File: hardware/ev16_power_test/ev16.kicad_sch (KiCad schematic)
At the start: 179 parts, among them CN1 Conn_05x02_Female, CN2 PJ-242, J1 USB_C_Receptacle, J10 Conn_01x03_Pin, J11 Conn_02x05_Counter_Clockwise, J2 Conn_01x02_Socket, J3 AudioJack4, J4 Conn_02x03_Odd_Even, J5 Conn_02x03_Odd_Even, J6 Conn_02x05_Counter_Clockwise, J7 Conn_02x05_Counter_Clockwise, J8 Conn_02x05_Counter_Clockwise, J9 Conn_02x05_Counter_Clockwise, Q1 2N7002, Q2 2N7002, Q3 2N7002, SW1 SW_SPDT, SW2 SW_Push, SW3 SW_Push, SW4 SW_Push, SW5 SW_Push, SW6 SW_Push, SW7 SW_Push, U1 BQ21040DBV, U10 STM32F405RGTx, U2 USBLC6-2P6, U3 STM32F072CBTx, U4 CH340C, U5 TPS63060, U6 WM8960CGEFL/RV, U7 ESP32-S3-WROOM-1, U8 M24C02-RMN6TP, U9 AMS1117-3.3, Y1 Crystal_GND24

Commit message: New linear regulator, ideal diodes, began working on the layout
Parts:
- removed C51, C52: 10u, Capacitor_SMD:C_0402_1005Metric, symbol Device:C
- removed D2, D3: 1N5819WS, Diode_SMD:D_SOD-323, symbol Device:D_Schottky
- removed J10: Conn_01x03_Pin, Connector_PinSocket_2.54mm:PinSocket_1x03_P2.54mm_Vertical_SMD_Pin1Left, symbol Connector:Conn_01x03_Pin
- removed U9: AMS1117-3.3, Package_TO_SOT_SMD:SOT-223-3_TabPin2, symbol Regulator_Linear:AMS1117-3.3
- added R47: 10k, Resistor_SMD:R_0402_1005Metric, symbol Device:R_Small_US
- added R53: 15k, Resistor_SMD:R_0402_1005Metric, symbol Device:R_Small_US
- added TP10, TP7, TP8, TP9: TestPoint, TestPoint:TestPoint_Pad_2.0x2.0mm, symbol Connector:TestPoint
- added U11: ME6211C28M5, Package_TO_SOT_SMD:SOT-23-5, symbol Regulator_Linear:ME6211C28M5
- added U9: TPS2116DRL, Package_TO_SOT_SMD:SOT-583-8, symbol Power_Management:TPS2116DRL
- C18, C7: value 10u -> 1u; JLCPCB Part # C307415 -> C52923
- TP1, TP2, TP3, TP4, TP5, TP6: footprint TestPoint:TestPoint_Pad_4.0x4.0mm -> TestPoint:TestPoint_Pad_2.0x2.0mm
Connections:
- net +3.3V: now also C7.1, U11.1 (V_{IN}), U11.3 (CE)
- net GND: now also R47.1, TP7.1, U11.2 (V_{SS}), U9.1 (GND)
- net GNDA: now also TP10.1
- net HP_L: now also TP8.1
- net MIC_P: now also TP9.1
- net VBUS: now also R53.2, U9.3 (VIN1), U9.5 (MODE)
- net at C12.1, J2.2 (Pin_2), R11.1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: now also U9.6 (VIN2)
- net VSYS: now reaches SW1.2 (B)
- net VSYS: now also R12.2, R14.1, TP3.1
- net at C18.1, L1.1: now also U11.5 (V_{OUT})
- new net: SW1.3 (C), U9.2 (VOUT), U9.7 (VOUT)
- new net: R47.2, R53.1, U9.4 (PR1)
- no-connect marks 57 -> 58
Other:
- note added: "BATTERY"
- moved on the sheet: C10, C11, C12, C14, C15, C16, C19, C20, C22, C24, C27, C29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

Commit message: finished laying out the board with the power changes
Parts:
- removed L1: 120Ω, Inductor_SMD:L_0603_1608Metric, symbol Device:FerriteBead
- added C51, C52: 100n, Capacitor_SMD:C_0402_1005Metric, symbol Device:C_Small
- added J10: Conn_01x03_Pin, Connector_PinHeader_1.00mm:PinHeader_1x03_P1.00mm_Vertical, symbol Connector:Conn_01x03_Socket
- C10: value 1u -> 100n; symbol Device:C -> Device:C_Small; JLCPCB Part # C52923 -> C85866
- C11: value 10n -> 100n; footprint Capacitor_SMD:C_0402_1005Metric -> Capacitor_SMD:C_0402_1005Metri; symbol Device:C -> Device:C_Small; JLCPCB Part # C15195 -> C85866
- C18, C7: symbol Device:C -> Device:C_Small
- C24, C27, C29, C30, C31, C35: value 10u -> 22u; JLCPCB Part # C17024 -> C5674
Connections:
- net +3.3V: now also U10.13 (VDDA), J10.1 (Pin_1); no longer C7.1, U11.1 (V_{IN}), U11.3 (CE)
- net +3.3VA: no longer U10.13 (VDDA)
- net GND: now also C51.2, C52.2; no longer C18.2, U11.2 (V_{SS})
- net GNDA: now also C18.2, U11.2 (V_{SS})
- net VSYS: now also J10.3 (Pin_3)
- net at C10.1, C11.1, R52.1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: now also C18.1, U11.5 (V_{OUT})
- new net: C51.1, C52.1, C7.1, J10.2 (Pin_2), U11.1 (V_{IN}), U11.3 (CE)
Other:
- moved on the sheet: C10, C11, C18, C7, NT1, R52, TP1, TP2, U11

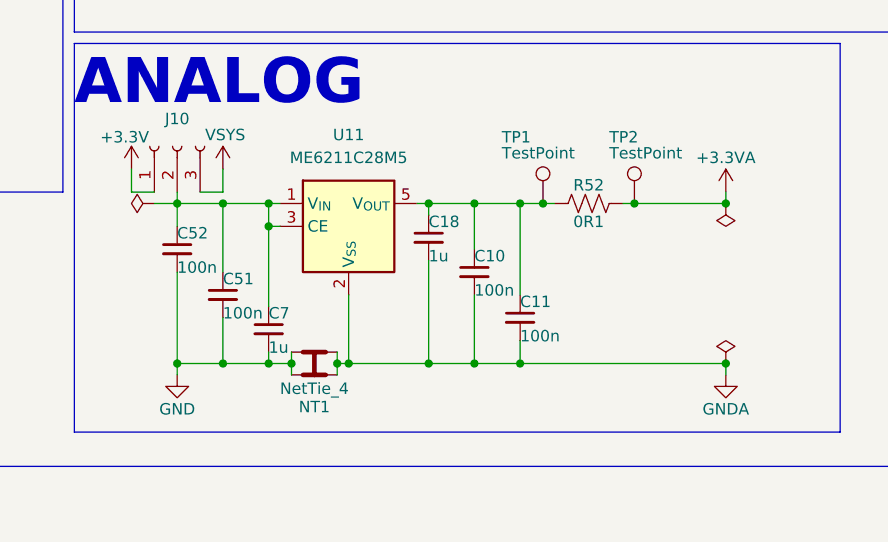
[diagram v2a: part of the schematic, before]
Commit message: Removed extra caps from linear power supply that wasn't needed
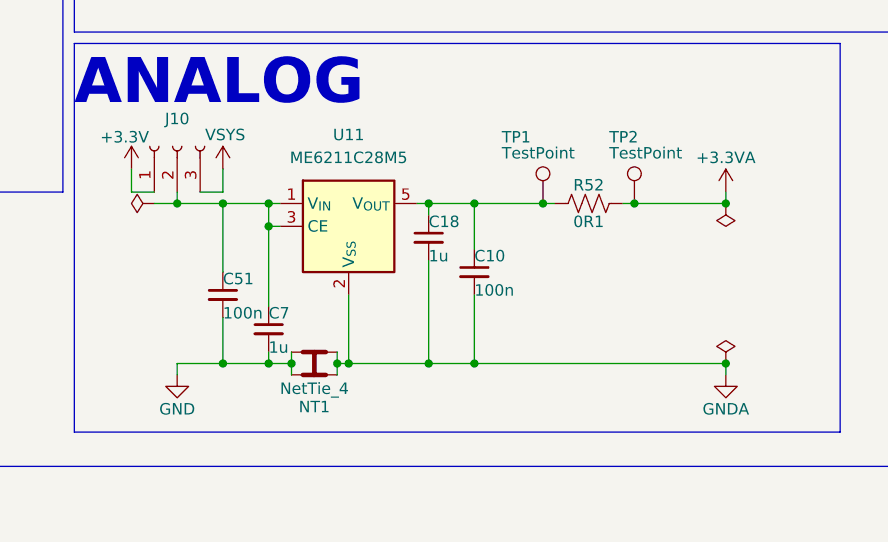
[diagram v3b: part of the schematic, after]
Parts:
- removed C11: 100n, Capacitor_SMD:C_0402_1005Metri, symbol Device:C_Small
- removed C52: 100n, Capacitor_SMD:C_0402_1005Metric, symbol Device:C_Small

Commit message: Changed linear regulator to XC6227C301MR-G and made a symbol for it. Added heat sink areas for the analog regulator
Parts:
- removed TP1, TP10, TP2, TP3, TP4, TP5, TP6, TP7, TP8, TP9: TestPoint, TestPoint:TestPoint_Pad_2.0x2.0mm, symbol Connector:TestPoint
- removed U11: ME6211C28M5, Package_TO_SOT_SMD:SOT-23-5, symbol Regulator_Linear:ME6211C28M5
- added J12, J13, J14, J15, J16, J17, J18, J19, J20, J21: Conn_01x01, Connector_PinHeader_2.54mm:PinHeader_1x01_P2.54mm_Vertical, symbol Connector_Generic:Conn_01x01
- added U12: XC6227C301MR-G, Package_TO_SOT_SMD:SOT-23-5, symbol Hactar_Symbols:XC6227C301MR-G
- J10: footprint Connector_PinHeader_1.00mm:PinHeader_1x03_P1.00mm_Vertical -> Connector_PinHeader_2.54mm:PinHeader_1x03_P2.54mm_Vertical; JLCPCB Part # C42379196 -> C146690
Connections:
- net +3.3V: now also J12.1 (Pin_1)
- net GND: now also J16.1 (Pin_1)
- net GNDA: now also J19.1 (Pin_1), U12.2 (VSS)
- net HP_L: now also J17.1 (Pin_1)
- net MIC_P: now also J18.1 (Pin_1)
- net VSYS: now also J15.1 (Pin_1)
- net at C22.1, C24.1, C27.1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: now also J13.1 (Pin_1)
- net at C14.1, C15.1, C16.1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: now also J14.1 (Pin_1)
- net at C10.1, C18.1, R52.1: now also J20.1 (Pin_1), U12.5 (VOUT)
- net AVIN: now reaches C51.1, C7.1, J10.2 (Pin_2)
- net AVIN: now also U12.1 (VIN), U12.3 (CE)
- net +3.3VA renamed +3.0VA
- net +3.0VA: now also J21.1 (Pin_1)
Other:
- moved on the sheet: C10, C18, R52
